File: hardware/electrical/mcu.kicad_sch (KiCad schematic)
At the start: 43 parts, among them J2 STDC14, SW1 SW_Push, SW2 SW_Push, U2 STM32F446ZET6, Y1 X322516MLB4SI, Y2 Q13FC1350000400

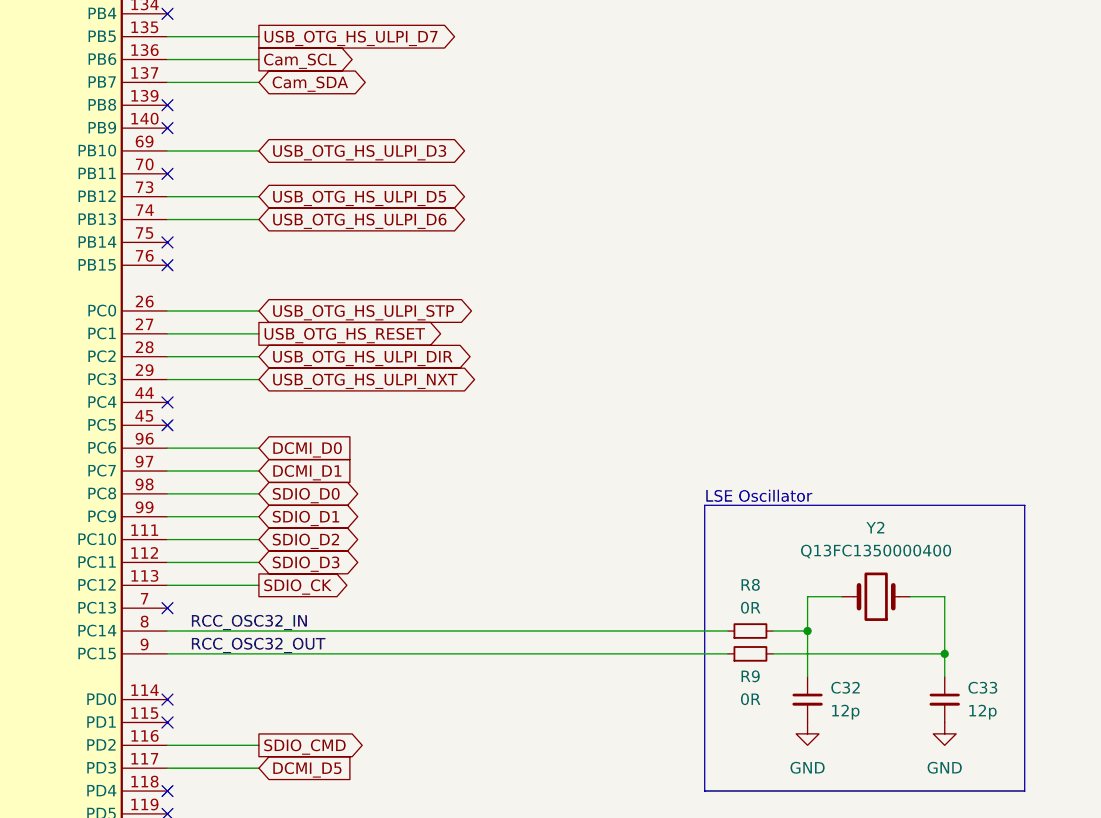
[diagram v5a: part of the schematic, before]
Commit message: Connect USB VBUS to WKUP1
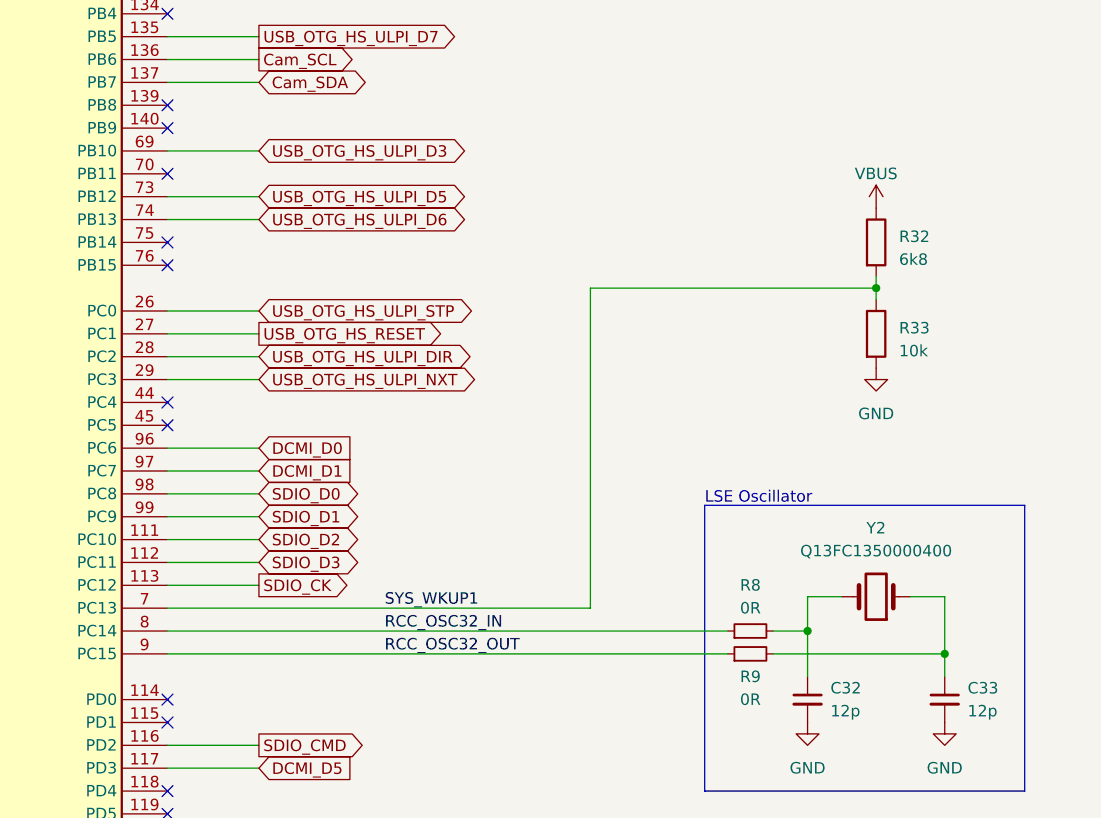
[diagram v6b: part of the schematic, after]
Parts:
- added R32: 6k8, symbol Device:R
- added R33: 10k, symbol Device:R
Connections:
- net GND: now also R33.2
- net SYS_WKUP1: now reaches U2.7 (PC13)
- net SYS_WKUP1: now also R32.2, R33.1
- new net VBUS: R32.1
- no-connect marks 73 -> 72
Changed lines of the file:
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@@
   (junction (at 152.4 25.4) (diameter 0) (color 0 0 0 0)
+  )
+  (junction (at 304.8 170.18) (diameter 0) (color 0 0 0 0)
   )
   (junction (at 96.52 121.92) (diameter 0) (color 0 0 0 0)
@@
   (no_connect (at 226.06 218.44))
   (no_connect (at 165.1 175.26))
-  (no_connect (at 226.06 205.74))
   (no_connect (at 165.1 236.22))
   (no_connect (at 165.1 132.08))
@@
     (stroke (width 0) (type default))
   )
+  (wire (pts (xy 304.8 168.91) (xy 304.8 170.18))
+    (stroke (width 0) (type default))
+  )
   (wire (pts (xy 187.96 76.2) (xy 185.42 76.2))
     (stroke (width 0) (type default))
@@
     (stroke (width 0) (type default))
   )
+  (wire (pts (xy 273.05 205.74) (xy 273.05 170.18))
+    (stroke (width 0) (type default))
+  )
   (wire (pts (xy 121.92 25.4) (xy 111.76 25.4))
     (stroke (width 0) (type default))
@@
     (stroke (width 0) (type default))
   )
+  (wire (pts (xy 273.05 170.18) (xy 304.8 170.18))
+    (stroke (width 0) (type default))
+  )
   (wire (pts (xy 182.88 25.4) (xy 172.72 25.4))
     (stroke (width 0) (type default))
@@
     (stroke (width 0) (type default))
   )
+  (wire (pts (xy 226.06 205.74) (xy 273.05 205.74))
+    (stroke (width 0) (type default))
+  )
   (wire (pts (xy 379.73 41.91) (xy 379.73 44.45))
     (stroke (width 0) (type default))
@@
   )
   (wire (pts (xy 203.2 76.2) (xy 203.2 78.74))
+    (stroke (width 0) (type default))
+  )
+  (wire (pts (xy 304.8 170.18) (xy 304.8 171.45))
     (stroke (width 0) (type default))
   )
@@
     (effects (font (size 1.27 1.27)) (justify left bottom))
   )
-  (label "RCC_OSC32_OUT" (at 228.6 210.82 0) (fields_autoplaced)
+  (label "SYS_WKUP1" (at 250.19 205.74 0) (fields_autoplaced)
+    (effects (font (size 1.27 1.27)) (justify left bottom))
+  )
+  (label "RCC_OSC32_OUT" (at 250.19 210.82 0) (fields_autoplaced)
     (effects (font (size 1.27 1.27)) (justify left bottom))
   )
@@
     (effects (font (size 1.27 1.27)) (justify right bottom))
   )
-  (label "RCC_OSC32_IN" (at 228.6 208.28 0) (fields_autoplaced)
+  (label "RCC_OSC32_IN" (at 250.19 208.28 0) (fields_autoplaced)
     (effects (font (size 1.27 1.27)) (justify left bottom))
   )
@@
     )
   )
+  (symbol (lib_id "Device:R") (at 304.8 165.1 0) (unit 1)
+    (in_bom yes) (on_board yes) (dnp no) (fields_autoplaced)
+    (property "Reference" "R32" (at 307.34 164.465 0)
+      (effects (font (size 1.27 1.27)) (justify left))
+    )
+    (property "Value" "6k8" (at 307.34 167.005 0)
+      (effects (font (size 1.27 1.27)) (justify left))
+    )
+    (property "Footprint" "" (at 303.022 165.1 90)
+      (effects (font (size 1.27 1.27)) hide)
+    )
+    (property "Datasheet" "~" (at 304.8 165.1 0)
+      (effects (font (size 1.27 1.27)) hide)
+    )
+    (pin "1")
+    (pin "2")
+    (instances
+      (project "3885"
+        (path "/7363a4f0-2da1-4086-abed-ea6709c3a185/239a74a2-fce8-4103-83ba-af4dbf21fb68"
+          (reference "R32") (unit 1)
+        )
+      )
+    )
+  )
   (symbol (lib_id "Device:R_Small") (at 290.83 208.28 90) (unit 1)
     (in_bom yes) (on_board yes) (dnp no)
@@
         (path "/7363a4f0-2da1-4086-abed-ea6709c3a185/239a74a2-fce8-4103-83ba-af4dbf21fb68"
           (reference "R8") (unit 1)
+        )
+      )
+    )
+  )
+  (symbol (lib_id "power:GND") (at 304.8 179.07 0) (unit 1)
+    (in_bom yes) (on_board yes) (dnp no) (fields_autoplaced)
+    (property "Reference" "#PWR084" (at 304.8 185.42 0)
+      (effects (font (size 1.27 1.27)) hide)
+    )
+    (property "Value" "GND" (at 304.8 184.15 0)
+      (effects (font (size 1.27 1.27)))
+    )
+    (property "Footprint" "" (at 304.8 179.07 0)
+      (effects (font (size 1.27 1.27)) hide)
+    )
+    (property "Datasheet" "" (at 304.8 179.07 0)
+      (effects (font (size 1.27 1.27)) hide)
+    )
+    (pin "1")
+    (instances
+      (project "3885"
+        (path "/7363a4f0-2da1-4086-abed-ea6709c3a185/239a74a2-fce8-4103-83ba-af4dbf21fb68"
+          (reference "#PWR084") (unit 1)
         )
       )
@@
         (path "/7363a4f0-2da1-4086-abed-ea6709c3a185/239a74a2-fce8-4103-83ba-af4dbf21fb68"
           (reference "#PWR016") (unit 1)
+        )
+      )
+    )
+  )
+  (symbol (lib_id "power:VBUS") (at 304.8 161.29 0) (unit 1)
+    (in_bom yes) (on_board yes) (dnp no) (fields_autoplaced)
+    (property "Reference" "#PWR083" (at 304.8 165.1 0)
+      (effects (font (size 1.27 1.27)) hide)
+    )
+    (property "Value" "VBUS" (at 304.8 157.48 0)
+      (effects (font (size 1.27 1.27)))
+    )
+    (property "Footprint" "" (at 304.8 161.29 0)
+      (effects (font (size 1.27 1.27)) hide)
+    )
+    (property "Datasheet" "" (at 304.8 161.29 0)
+      (effects (font (size 1.27 1.27)) hide)
+    )
+    (pin "1")
+    (instances
+      (project "3885"
+        (path "/7363a4f0-2da1-4086-abed-ea6709c3a185/239a74a2-fce8-4103-83ba-af4dbf21fb68"
+          (reference "#PWR083") (unit 1)
         )
       )
@@
         )
       )
+    )
+  )
+  (symbol (lib_id "Device:R") (at 304.8 175.26 0) (unit 1)
+    (in_bom yes) (on_board yes) (dnp no) (fields_autoplaced)
+    (property "Reference" "R33" (at 307.34 174.625 0)
+      (effects (font (size 1.27 1.27)) (justify left))
+    )
+    (property "Value" "10k" (at 307.34 177.165 0)
+      (effects (font (size 1.27 1.27)) (justify left))
+    )
+    (property "Footprint" "" (at 303.022 175.26 90)
+      (effects (font (size 1.27 1.27)) hide)
+    )
+    (property "Datasheet" "~" (at 304.8 175.26 0)
+      (effects (font (size 1.27 1.27)) hide)
+    )
+    (pin "1")
+    (pin "2")
+    (instances
+      (project "3885"
+        (path "/7363a4f0-2da1-4086-abed-ea6709c3a185/239a74a2-fce8-4103-83ba-af4dbf21fb68"
+          (reference "R33") (unit 1)
+        )
+      )

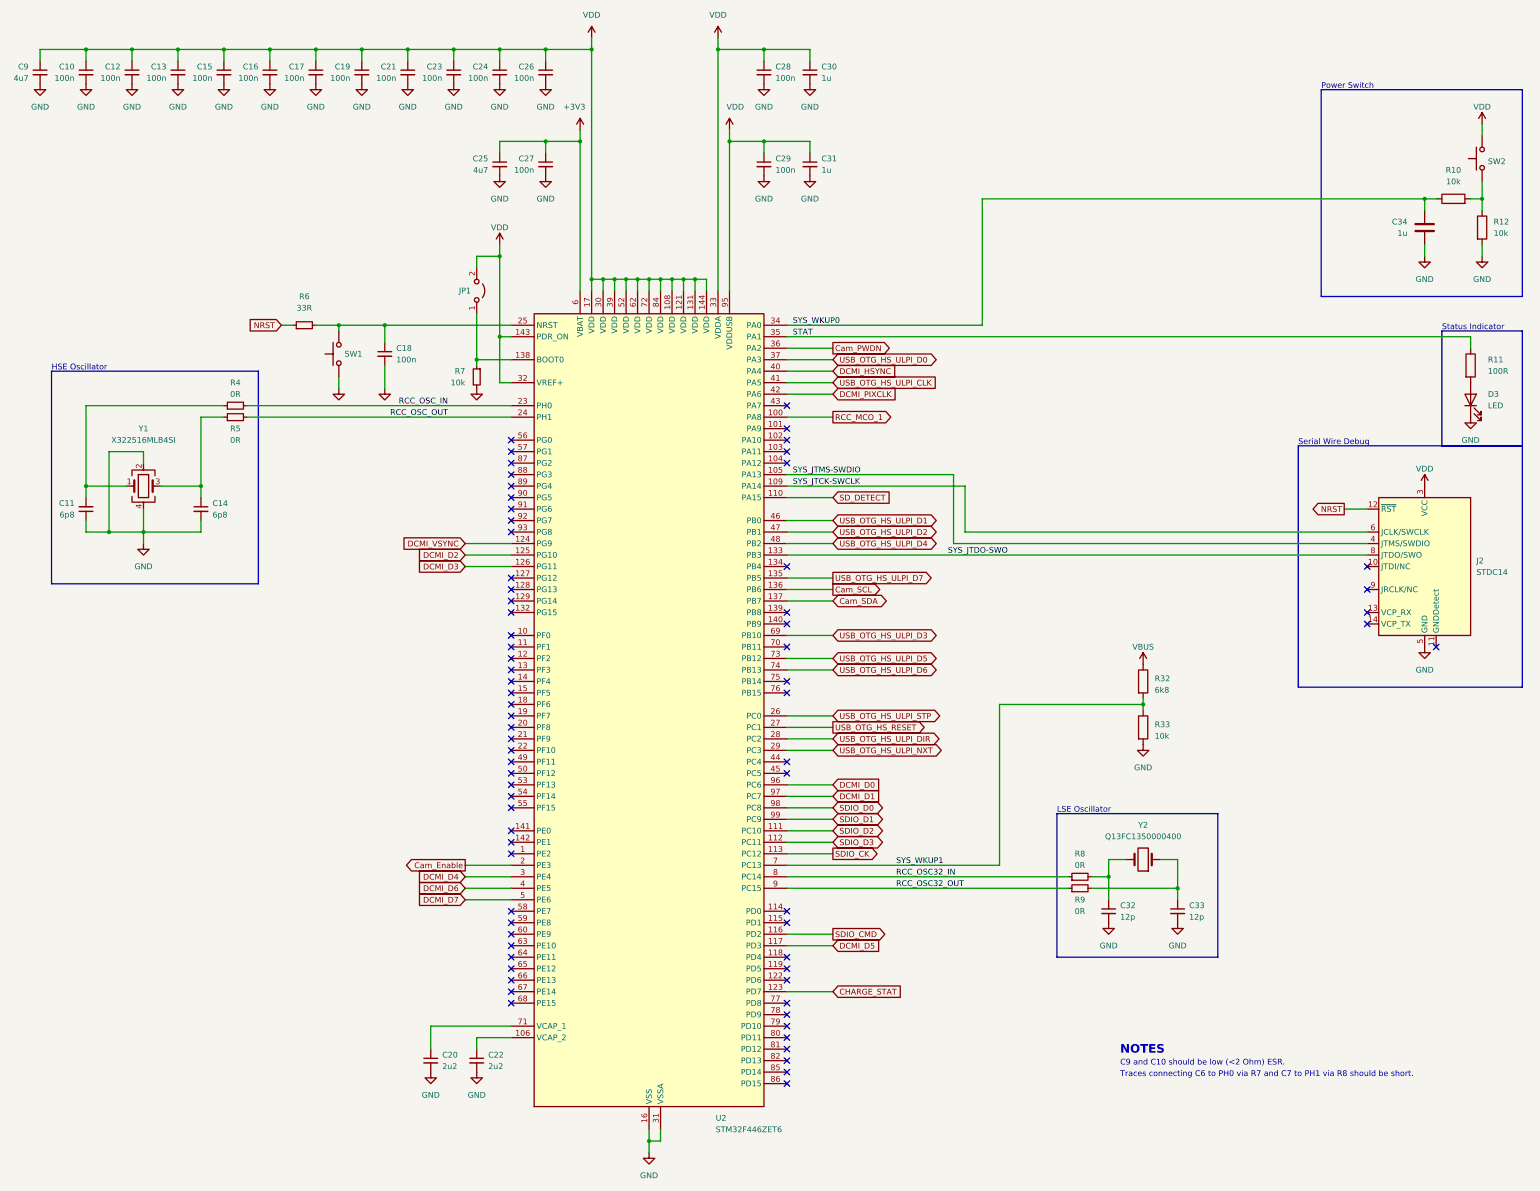
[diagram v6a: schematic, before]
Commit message: Change microcontroller to STM32F446VET6
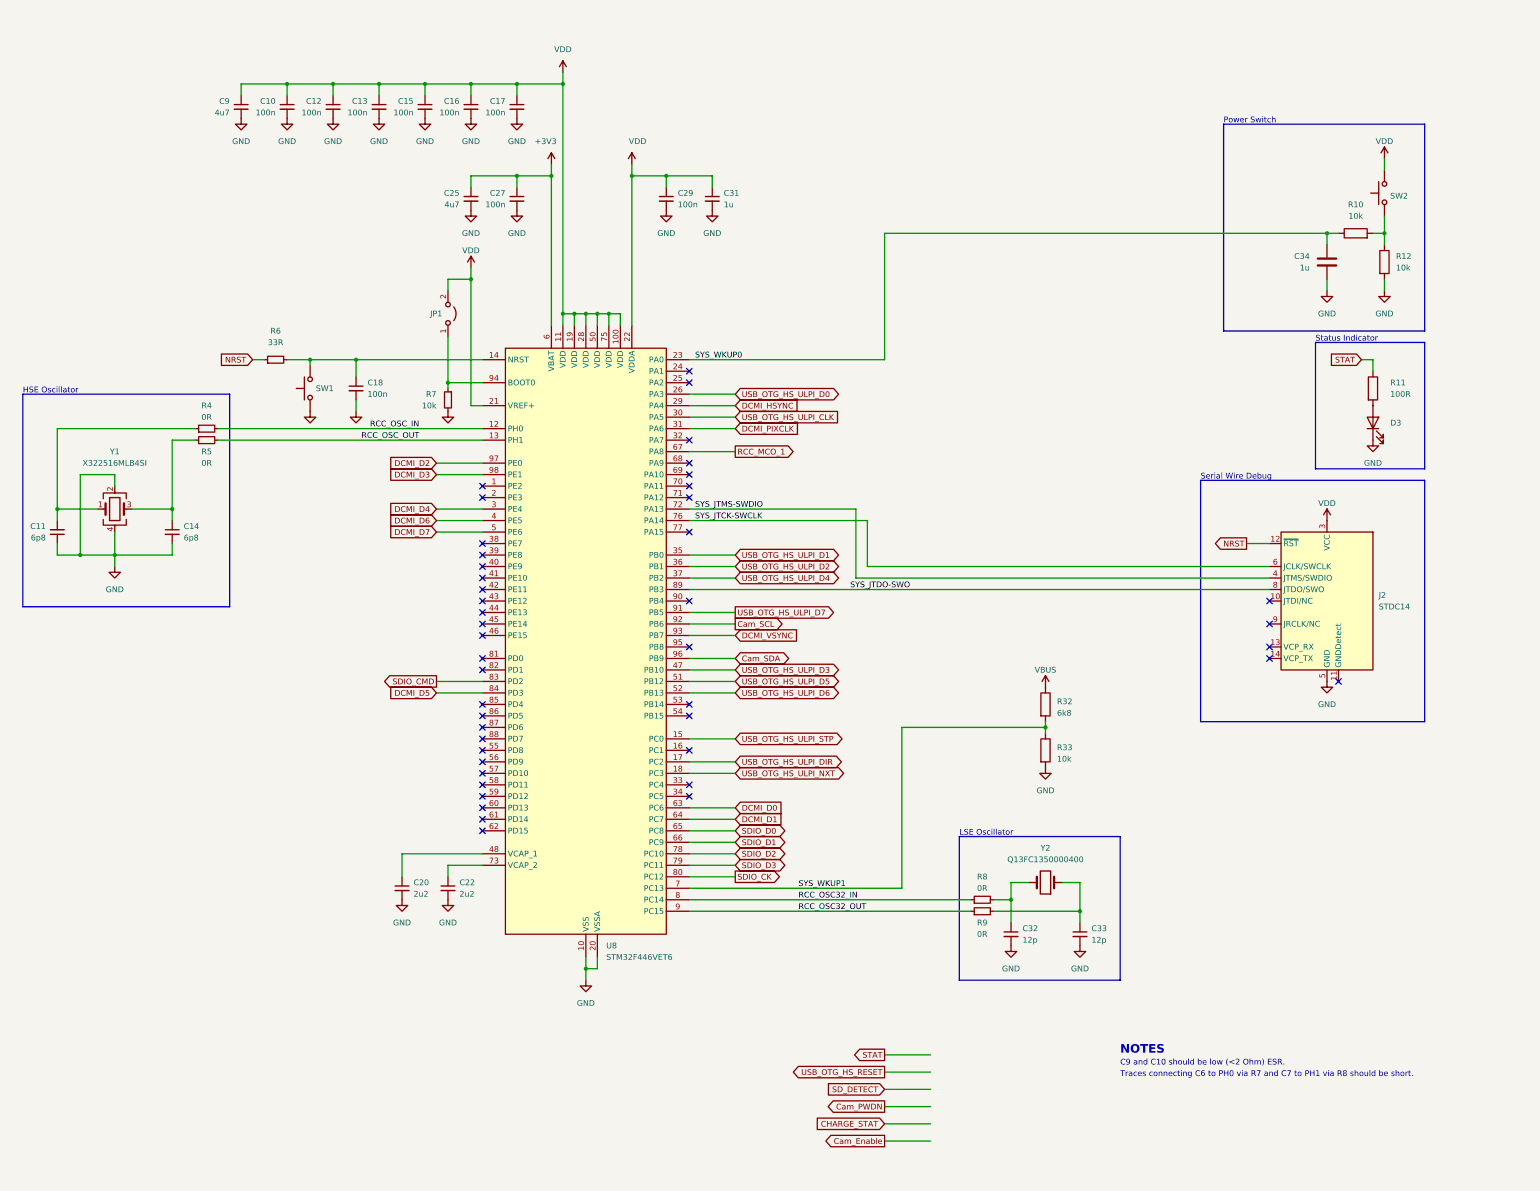
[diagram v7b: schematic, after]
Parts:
- removed C19, C21, C23, C24, C26, C28: 100n, symbol Device:C_Small
- removed C30: 1u, symbol Device:C_Small
- removed U2: STM32F446ZET6, Package_QFP:LQFP-144_20x20mm_P0.5mm, symbol MCU_ST_STM32F4:STM32F446ZETx
- added U8: STM32F446VET6, Package_QFP:LQFP-100_14x14mm_P0.5mm, symbol MCU_ST_STM32F4:STM32F446VETx
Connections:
- net +3V3: now also U8.6 (VBAT)
- net Cam_SCL: now also U8.92 (PB6)
- net Cam_SDA: now also U8.96 (PB9)
- net DCMI_D0: now also U8.63 (PC6)
- net DCMI_D1: now also U8.64 (PC7)
- net DCMI_D2: now also U8.97 (PE0)
- net DCMI_D3: now also U8.98 (PE1)
- net DCMI_D4: now also U8.3 (PE4)
- net DCMI_D5: now also U8.84 (PD3)
- net DCMI_D6: now also U8.4 (PE5)
- net DCMI_D7: now also U8.5 (PE6)
- net DCMI_HSYNC: now also U8.29 (PA4)
- net DCMI_PIXCLK: now also U8.31 (PA6)
- net DCMI_VSYNC: now also U8.93 (PB7)
- net GND: now also U8.10 (VSS), U8.20 (VSSA), U8.27 (VSS), U8.49 (VSS), U8.74 (VSS), U8.99 (VSS)
- net RCC_MCO_1: now also U8.67 (PA8)
- net RCC_OSC32_IN: now also U8.8 (PC14)
- net RCC_OSC32_OUT: now also U8.9 (PC15)
- net RCC_OSC_IN: now also U8.12 (PH0)
- net RCC_OSC_OUT: now also U8.13 (PH1)
- net SDIO_CK: now also U8.80 (PC12)
- net SDIO_CMD: now also U8.83 (PD2)
- net SDIO_D0: now also U8.65 (PC8)
- net SDIO_D1: now also U8.66 (PC9)
- net SDIO_D2: now also U8.78 (PC10)
- net SDIO_D3: now also U8.79 (PC11)
- net SYS_JTCK-SWCLK: now also U8.76 (PA14)
- net SYS_JTDO-SWO: now also U8.89 (PB3)
- net SYS_JTMS-SWDIO: now also U8.72 (PA13)
- net SYS_WKUP0: now also U8.23 (PA0)
- net SYS_WKUP1: now also U8.7 (PC13)
- net USB_OTG_HS_ULPI_CLK: now also U8.30 (PA5)
- net USB_OTG_HS_ULPI_D0: now also U8.26 (PA3)
- net USB_OTG_HS_ULPI_D1: now also U8.35 (PB0)
- net USB_OTG_HS_ULPI_D2: now also U8.36 (PB1)
- net USB_OTG_HS_ULPI_D3: now also U8.47 (PB10)
- net USB_OTG_HS_ULPI_D4: now also U8.37 (PB2)
- net USB_OTG_HS_ULPI_D5: now also U8.51 (PB12)
- net USB_OTG_HS_ULPI_D6: now also U8.52 (PB13)
- net USB_OTG_HS_ULPI_D7: now also U8.91 (PB5)
- net USB_OTG_HS_ULPI_DIR: now also U8.17 (PC2)
- net USB_OTG_HS_ULPI_NXT: now also U8.18 (PC3)
- net USB_OTG_HS_ULPI_STP: now also U8.15 (PC0)
- net VDD: now also U8.100 (VDD), U8.11 (VDD), U8.19 (VDD), U8.21 (VREF+), U8.22 (VDDA), U8.28 (VDD), U8.50 (VDD), U8.75 (VDD)
- net at C20.1: now also U8.48 (VCAP_1)
- net at JP1.1 (A), R7.1: now also U8.94 (BOOT0)
- net at C18.1, R6.2, SW1.2: now also U8.14 (NRST)
- net at C22.1: now also U8.73 (VCAP_2)
- no-connect marks 72 -> 45
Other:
- moved on the sheet: C10, C11, C12, C13, C14, C15, C16, C17, C18, C20, C22, C25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
